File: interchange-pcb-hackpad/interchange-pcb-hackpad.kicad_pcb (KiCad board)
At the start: 2 copper layers, 120 x 95 mm, 107 parts, among them J1 MagnetR, J2 MagnetL, J3 TRRS_R, J4 TRRS_L, J5 SSD1306, J6 Conn_01x06, U1 Seeeduino Xiao rp2040, U2 PCA9555PW, U3 PCA9555PW

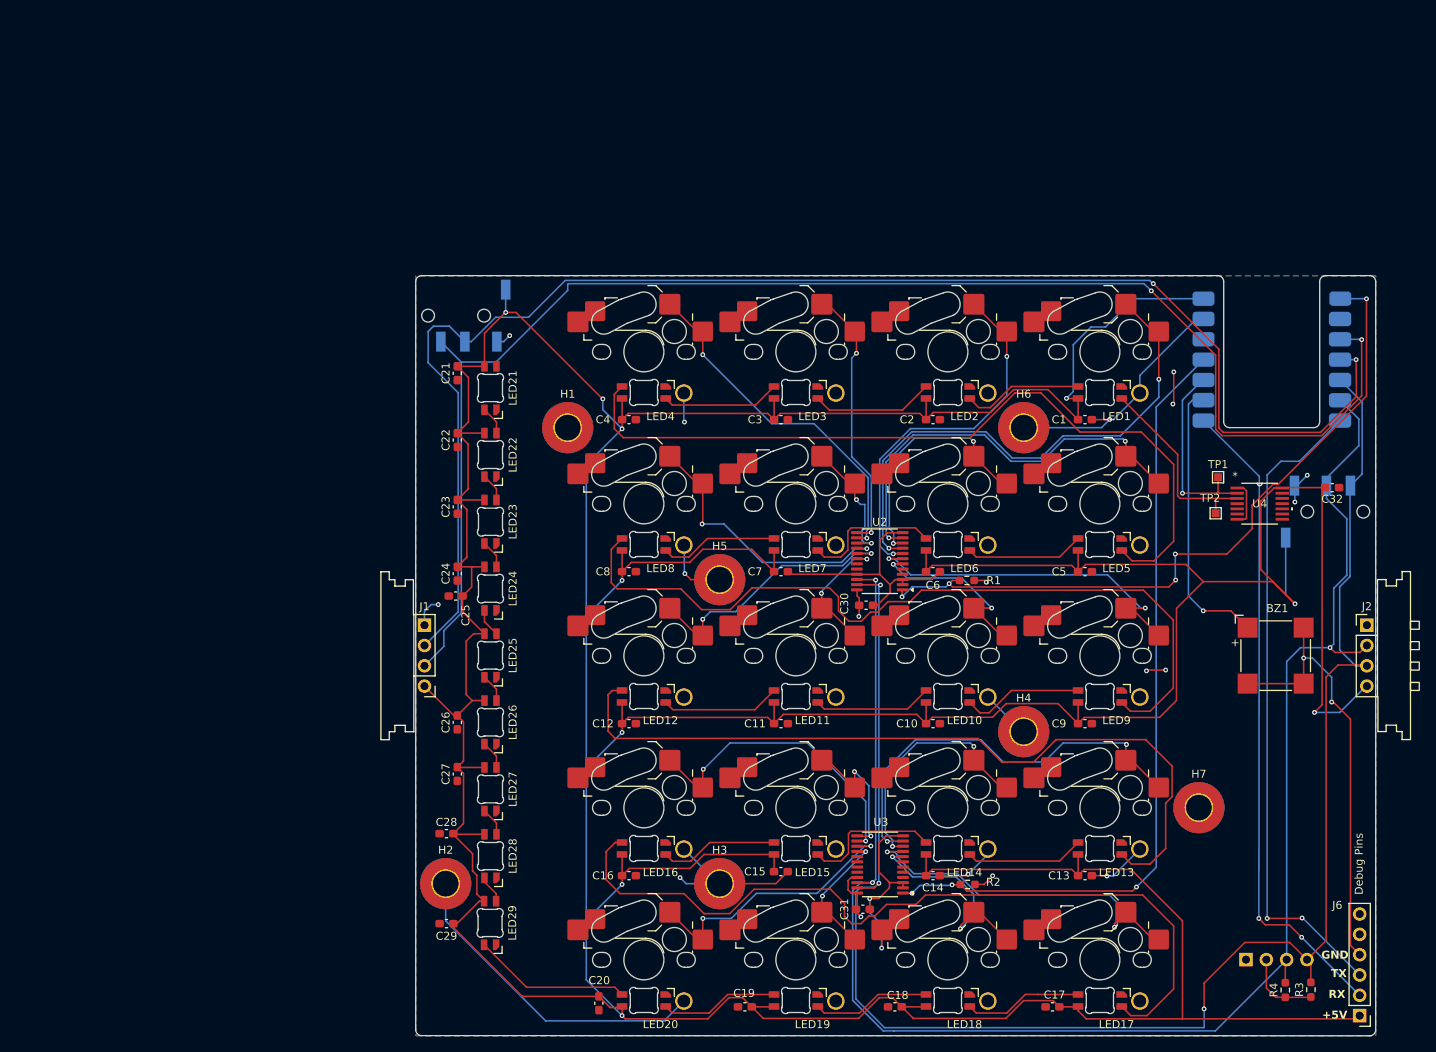
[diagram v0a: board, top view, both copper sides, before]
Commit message: feat: create schematic for interchange-pcb-hackpad
and fix minor spacing issues with capaicitors in interchange-pcb-right
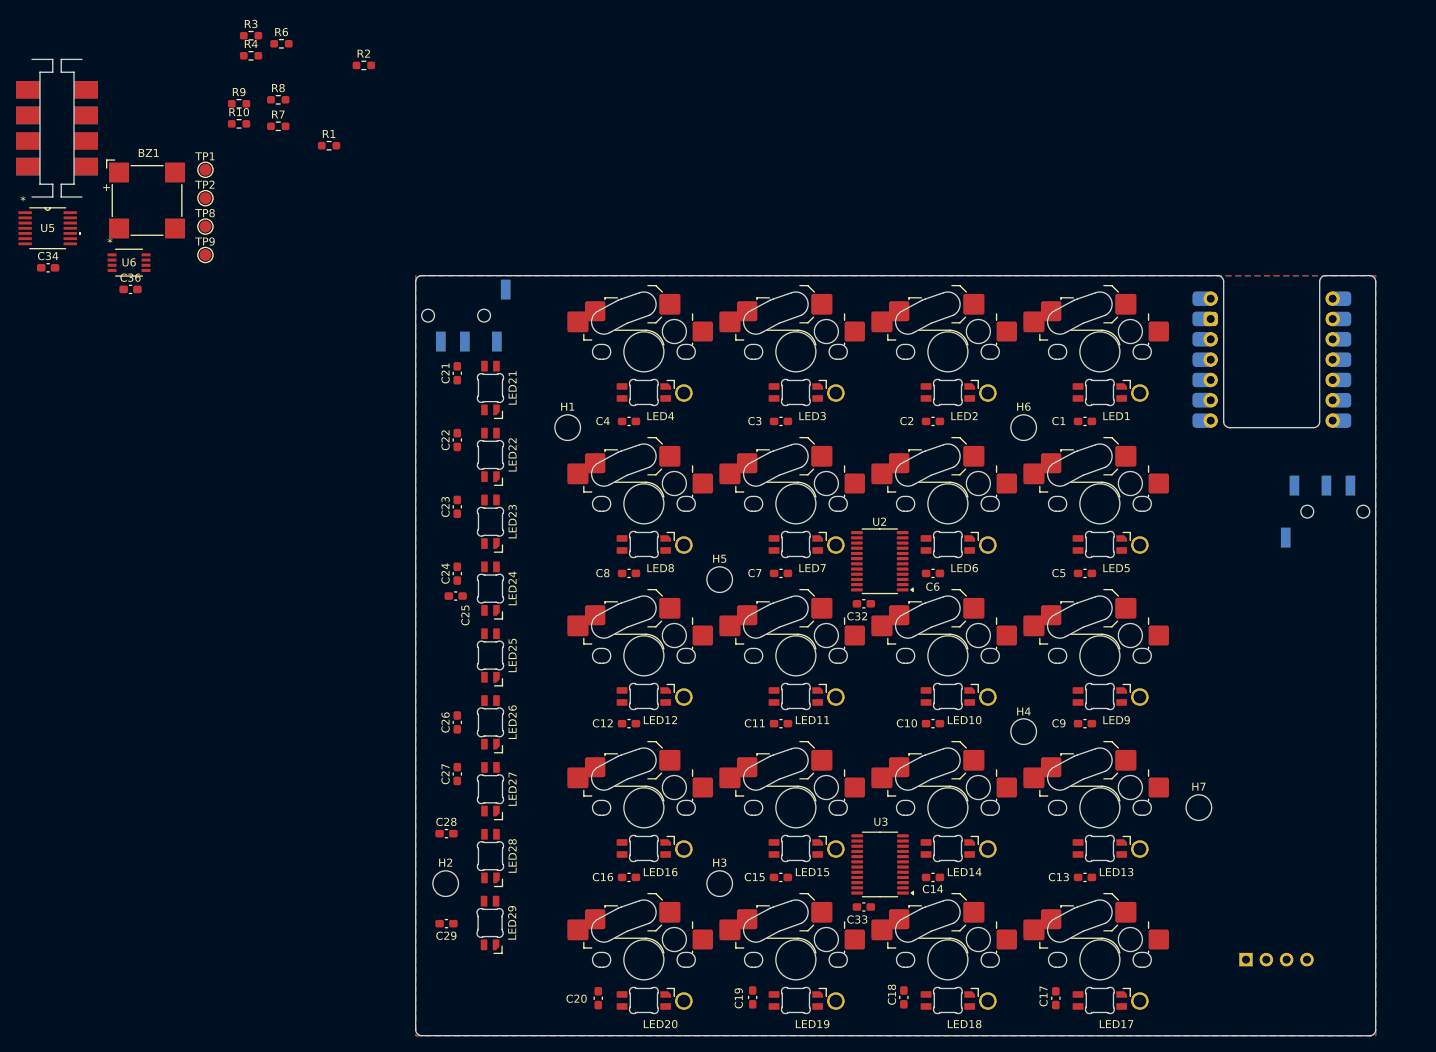
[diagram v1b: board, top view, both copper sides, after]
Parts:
- removed C30, C31: 100nF, Capacitor_SMD:C_0603_1608Metric_Pad1.08x0.95mm_HandSolder
- removed J6: Conn_01x06, Connector_PinHeader_2.54mm:PinHeader_1x06_P2.54mm_Vertical
- removed OSHW: OSHW-Logo2_7.3x6mm_SilkScreen, Symbol:OSHW-Logo2_7.3x6mm_SilkScreen
- removed U4: , CustomFootprints:SN74AHCT125PWR
- removed WEEE: WEEE-Logo_4.2x6mm_SilkScreen, Symbol:WEEE-Logo_4.2x6mm_SilkScreen
- added C33: 100nF, Capacitor_SMD:C_0603_1608Metric_Pad1.08x0.95mm_HandSolder, F.Cu at (140.6, 125.2)
- added C34: 100nF, Capacitor_SMD:C_0603_1608Metric_Pad1.08x0.95mm_HandSolder, F.Cu at (38.6, 45.3)
- added C36: 100nF, Capacitor_SMD:C_0603_1608Metric_Pad1.08x0.95mm_HandSolder, F.Cu at (48.9, 48.0)
- added R10: 2.2k, Resistor_SMD:R_0603_1608Metric_Pad0.98x0.95mm_HandSolder, F.Cu at (62.5, 27.3)
- added R6: 10k, Resistor_SMD:R_0603_1608Metric_Pad0.98x0.95mm_HandSolder, F.Cu at (67.8, 17.3)
- added R7: 2.2k, Resistor_SMD:R_0603_1608Metric_Pad0.98x0.95mm_HandSolder, F.Cu at (67.4, 27.6)
- added R8: 2.2k, Resistor_SMD:R_0603_1608Metric_Pad0.98x0.95mm_HandSolder, F.Cu at (67.4, 24.3)
- added R9: 2.2k, Resistor_SMD:R_0603_1608Metric_Pad0.98x0.95mm_HandSolder, F.Cu at (62.5, 24.8)
- added TP8: TestPoint, TestPoint:TestPoint_Pad_D1.5mm, F.Cu at (58.3, 40.1)
- added TP9: TestPoint, TestPoint:TestPoint_Pad_D1.5mm, F.Cu at (58.3, 43.7)
- added U5: , CustomFootprints:SN74AHCT125PWR, F.Cu at (38.6, 40.4)
- added U6: TCA4307DGKR, CustomFootprints:SOIC8_DGK_TEX, F.Cu at (48.8, 44.7)
- H1, H2, H3, H4, H5, H6, H7: footprint MountingHole:MountingHole_3.2mm_M3_Pad_TopBottom -> MountingHole:MountingHole_3.2mm_M3
- J1: value MagnetR -> Conn_01x04; footprint CustomFootprints:5358_mag_connector_1x4_pads -> CustomFootprints:MagneticSlot_Right
- J2: value MagnetL -> Conn_01x04; footprint CustomFootprints:5358_mag_connector_1x4_pins -> CustomFootprints:MagneticSlot_Left
- J3: value TRRS_R -> TRRS_L
- J4: value TRRS_L -> TRRS_R
- R1, R2: value 10k -> 2.2k
- R3, R4: value 2.2k -> 10k
- TP1: value NPIXEL_SHIFT -> TestPoint; footprint TestPoint:TestPoint_Pad_1.0x1.0mm -> TestPoint:TestPoint_Pad_D1.5mm
- TP2: value NPIXEL_IN -> TestPoint; footprint TestPoint:TestPoint_Pad_1.0x1.0mm -> TestPoint:TestPoint_Pad_D1.5mm
- moved R3 178.2 mm to (64.0, 16.3), turned to 0 degrees
- moved R4 174.2 mm to (64.0, 18.8), turned to 0 degrees
- moved J2 173.6 mm to (42.9, 27.9)
- moved BZ1 152.1 mm to (51.0, 36.9)
- moved TP1 132.3 mm to (58.3, 33.0)
- moved TP2 132.3 mm to (58.3, 36.6)
- moved R2 127.2 mm to (78.1, 20.0), turned to 0 degrees
- moved R1 96.5 mm to (73.8, 30.0), turned to 0 degrees
- moved J1 82.2 mm to (36.6, 27.9)
- moved C32 60.3 mm to (140.6, 87.3), turned to 0 degrees
- moved C18 1.63 mm to (145.6, 136.5), turned to 90 degrees
- moved C19 1.53 mm to (126.7, 136.5), turned to 90 degrees
- moved C17 1.16 mm to (164.6, 136.6), turned to 90 degrees
- moved C15 0.72 mm to (130.2, 121.5)
- moved C20 0.64 mm to (107.4, 136.6)
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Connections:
- net /KEY_PIXEL_INPUT renamed /SHIFTER_OUTPUT
- net /KEY_PIXEL_SHIFT_INPUT renamed /SHIFTER_INPUT
- C32 pad 2: VBUS -> +3V3
- J1 pad 1: GND -> /I2C_BUS_SDA
- J1 pad 2: /I2C0_SCL -> /I2C_BUS_SCL
- J1 pad 3: /I2C0_SDA -> GND
- J2 pad 1: GND -> /I2C_BUS_SDA
- J2 pad 2: /I2C1_SCL -> /I2C_BUS_SCL
- J2 pad 3: /I2C1_SDA -> GND
- J3 pad R1: /I2C0_SCL -> /I2C_BUS_SDA
- J3 pad R2: /I2C0_SDA -> /I2C_BUS_SCL
- J4 pad R1: /I2C1_SCL -> /I2C_BUS_SDA
- J4 pad R2: /I2C1_SDA -> /I2C_BUS_SCL
- J5 pad 3: /I2C1_SCL -> /I2C0_SCL
- J5 pad 4: /I2C1_SDA -> /I2C0_SDA
- LED21 pad 2: unconnected-(LED21-DOUT-Pad2) -> Net-(LED21-DOUT)
- LED21 pad 3: Net-(LED21-DIN) -> Net-(LED20-DOUT)
- LED22 pad 2: Net-(LED21-DIN) -> Net-(LED22-DOUT)
- LED22 pad 3: Net-(LED22-DIN) -> Net-(LED21-DOUT)
- LED23 pad 2: Net-(LED22-DIN) -> Net-(LED23-DOUT)
- LED23 pad 3: Net-(LED23-DIN) -> Net-(LED22-DOUT)
- LED24 pad 2: Net-(LED23-DIN) -> Net-(LED24-DOUT)
- LED24 pad 3: Net-(LED24-DIN) -> Net-(LED23-DOUT)
- LED25 pad 2: Net-(LED24-DIN) -> Net-(LED25-DOUT)
- LED25 pad 3: Net-(LED25-DIN) -> Net-(LED24-DOUT)
- LED26 pad 2: Net-(LED25-DIN) -> Net-(LED26-DOUT)
- LED26 pad 3: Net-(LED26-DIN) -> Net-(LED25-DOUT)
- LED27 pad 2: Net-(LED26-DIN) -> Net-(LED27-DOUT)
- LED27 pad 3: Net-(LED27-DIN) -> Net-(LED26-DOUT)
- LED28 pad 2: Net-(LED27-DIN) -> Net-(LED28-DOUT)
- LED28 pad 3: Net-(LED28-DIN) -> Net-(LED27-DOUT)
- LED29 pad 2: Net-(LED28-DIN) -> /RGB LED Array/Output
- LED29 pad 3: Net-(LED20-DOUT) -> Net-(LED28-DOUT)
- R1 pad 2: /EXPANDER1_INT -> /I2C0_SCL
- R2 pad 2: /EXPANDER2_INT -> /I2C0_SDA
- R3 pad 2: /I2C1_SDA -> /EXPANDER1_INT
- R4 pad 2: /I2C1_SCL -> /EXPANDER2_INT
- U1 pad 1: /EXPANDER1_INT -> unconnected-(U1-P26-Pad1)
- U1 pad 11: /EXPANDER2_INT -> /BUZZER
- U1 pad 13: /BUZZER -> /EXPANDER2_INT
- U1 pad 14: /UART0_RX -> /EXPANDER1_INT
- U1 pad 7: /UART0_TX -> /I2C1_RDY
- U2 pad 22: /I2C1_SCL -> /I2C0_SCL
- U2 pad 23: /I2C1_SDA -> /I2C0_SDA
- U3 pad 22: /I2C1_SCL -> /I2C0_SCL
- U3 pad 23: /I2C1_SDA -> /I2C0_SDA
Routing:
- net VBUS: track 801.7 -> 0.00 mm, vias 10 -> 0
- net GND: track 254.5 -> 0.00 mm, vias 14 -> 0
- net /I2C1_SDA: track 211.9 -> 0.00 mm, vias 3 -> 0
- net /I2C1_SCL: track 205.6 -> 0.00 mm, vias 3 -> 0
- net /I2C0_SDA: track 185.6 -> 0.00 mm, vias 2 -> 0
- net /I2C0_SCL: track 185.1 -> 0.00 mm, vias 2 -> 0
- net Net-(LED16-DOUT): track 102.0 -> 0.00 mm
- net Net-(LED8-DOUT): track 101.4 -> 0.00 mm
- net Net-(LED4-DOUT): track 99.7 -> 0.00 mm
- net /EXPANDER2_INT: track 99.7 -> 0.00 mm, vias 3 -> 0
- net Net-(LED12-DOUT): track 98.6 -> 0.00 mm
- net /EXPANDER1_INT: track 90.5 -> 0.00 mm, vias 5 -> 0
- net /UART0_TX: track 82.1 -> 0.00 mm, vias 2 -> 0
- net /UART0_RX: track 81.9 -> 0.00 mm, vias 2 -> 0
- net /KEY1: track 67.1 -> 0.00 mm, vias 2 -> 0
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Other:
- board text removed: "+5V"
- board text removed: "Debug Pins"
- board text removed: "RX"
- board text removed: "TX"

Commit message: feat(right): add LCSC part numbers to schematics
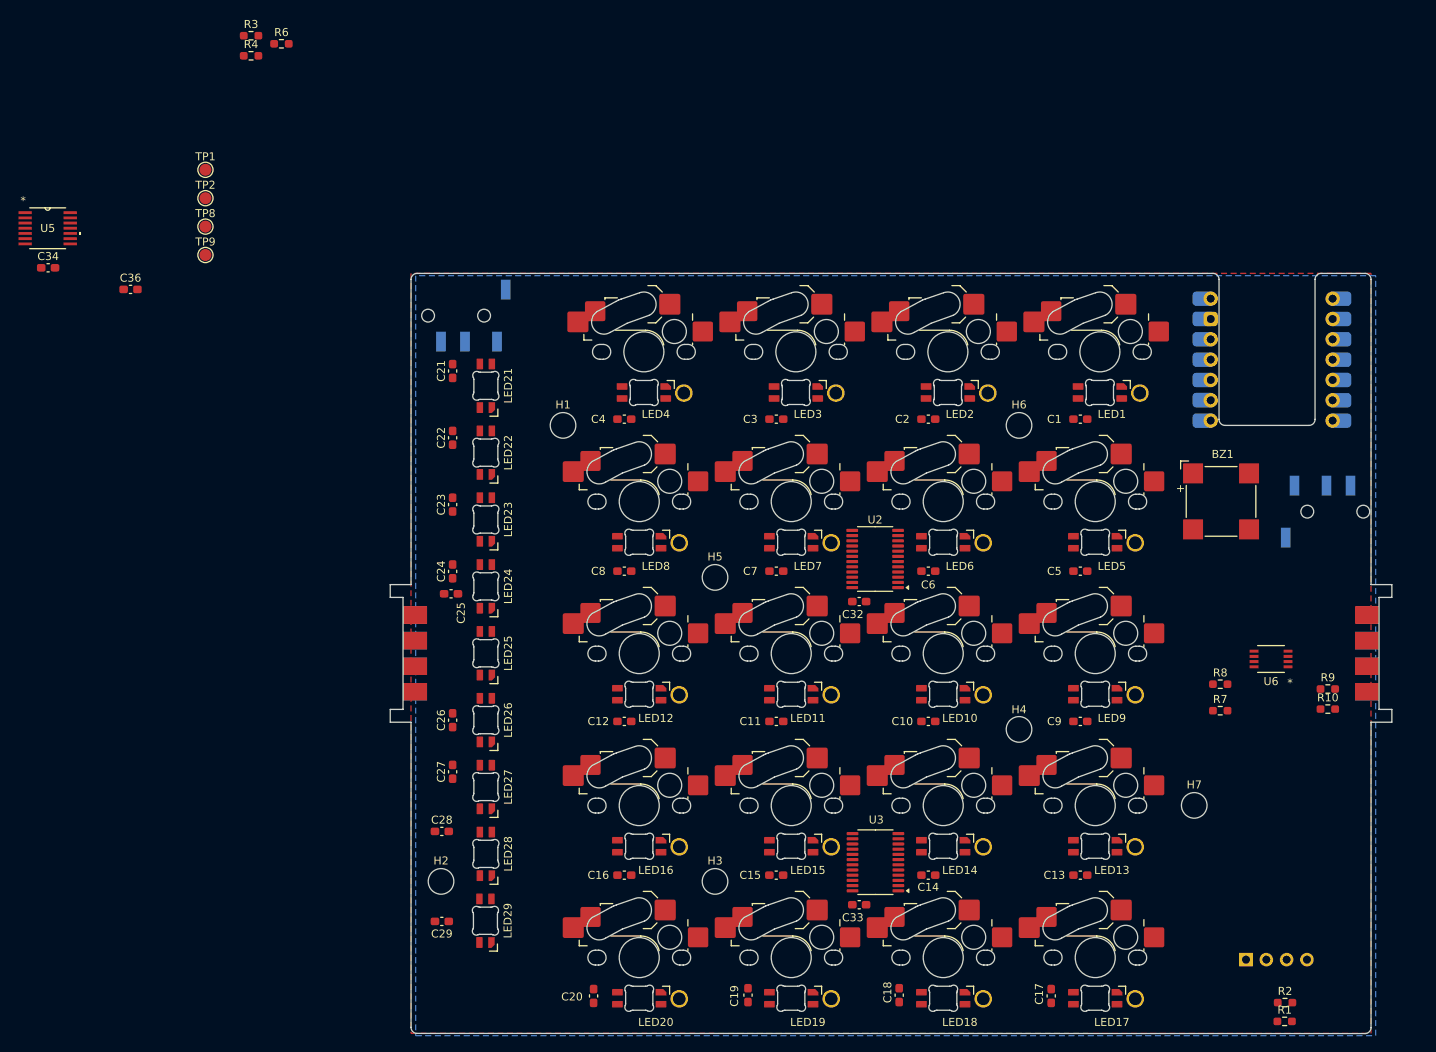
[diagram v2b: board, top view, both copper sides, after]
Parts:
- moved J1 179.8 mm to (204.0, 93.5)
- moved R2 164.3 mm to (193.2, 137.2)
- moved R1 162.0 mm to (193.2, 139.5)
- moved R10 154.5 mm to (198.6, 100.5)
- moved R9 154.5 mm to (198.6, 98.0)
- moved U6 151.1 mm to (191.5, 94.2), turned to 180 degrees
- moved BZ1 139.4 mm to (185.2, 74.5)
- moved R7 138.6 mm to (185.2, 100.7)
- moved R8 138.6 mm to (185.2, 97.3)
- moved J2 77.5 mm to (84.0, 93.5)
- moved C1 0.64 mm to (167.7, 64.2)
- moved C10 0.64 mm to (148.7, 102.0)
- moved C11 0.64 mm to (129.7, 102.0)
- moved C12 0.64 mm to (110.7, 102.0)
- moved C13 0.64 mm to (167.7, 121.2)
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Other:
- outline, holes or cut-outs redrawn
